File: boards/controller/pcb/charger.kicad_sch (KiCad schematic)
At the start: 44 parts, among them J4001 Battery, Q4001 BSS138, U4001 3.6, U4002 BQ25792RQMR

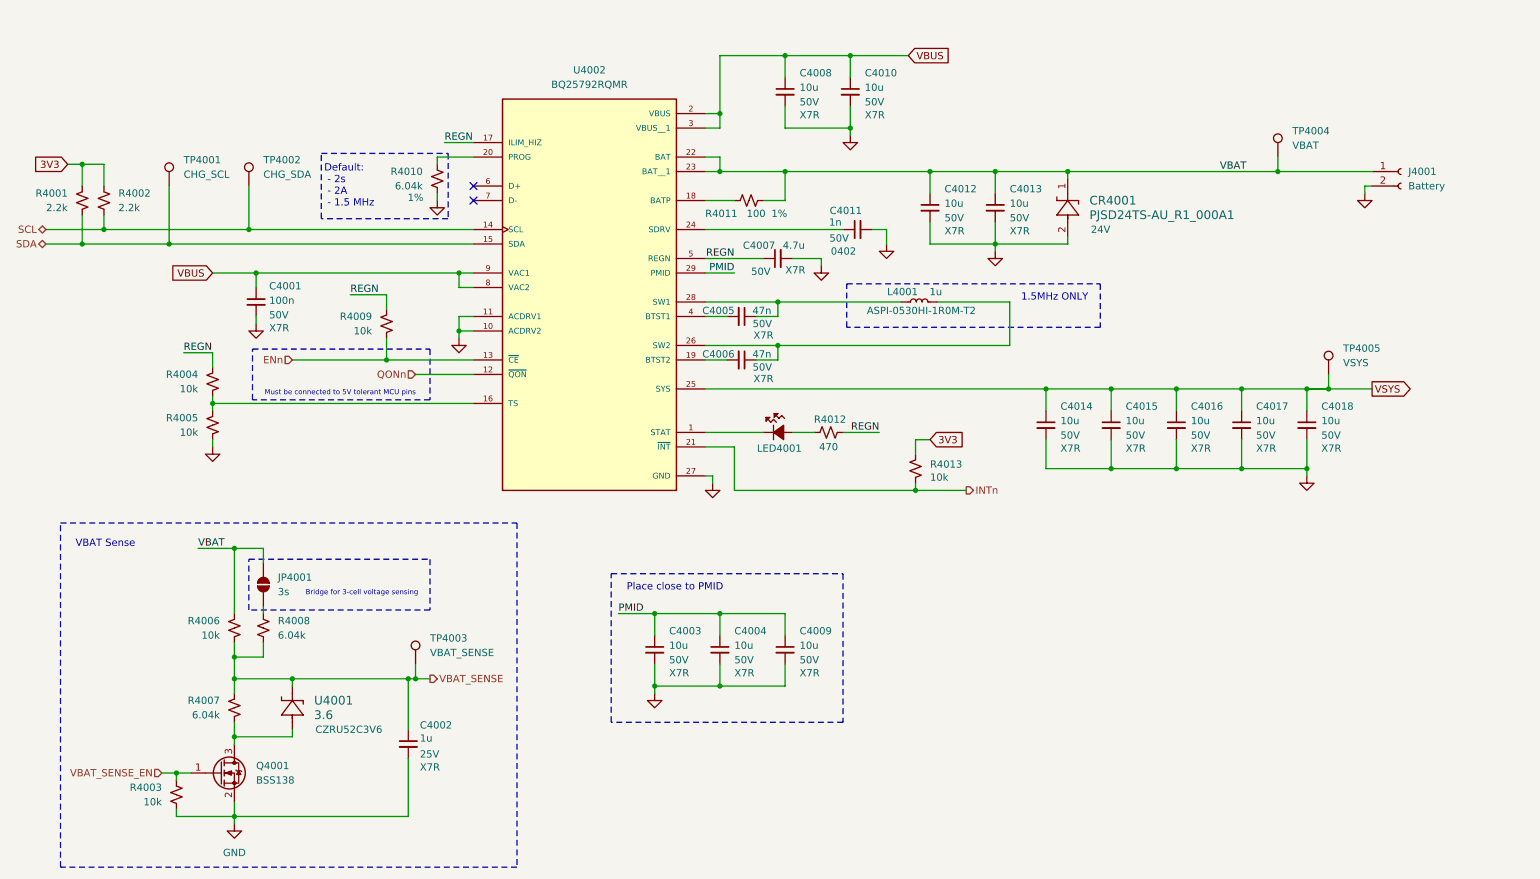
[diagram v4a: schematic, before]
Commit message: controller: Update BOM
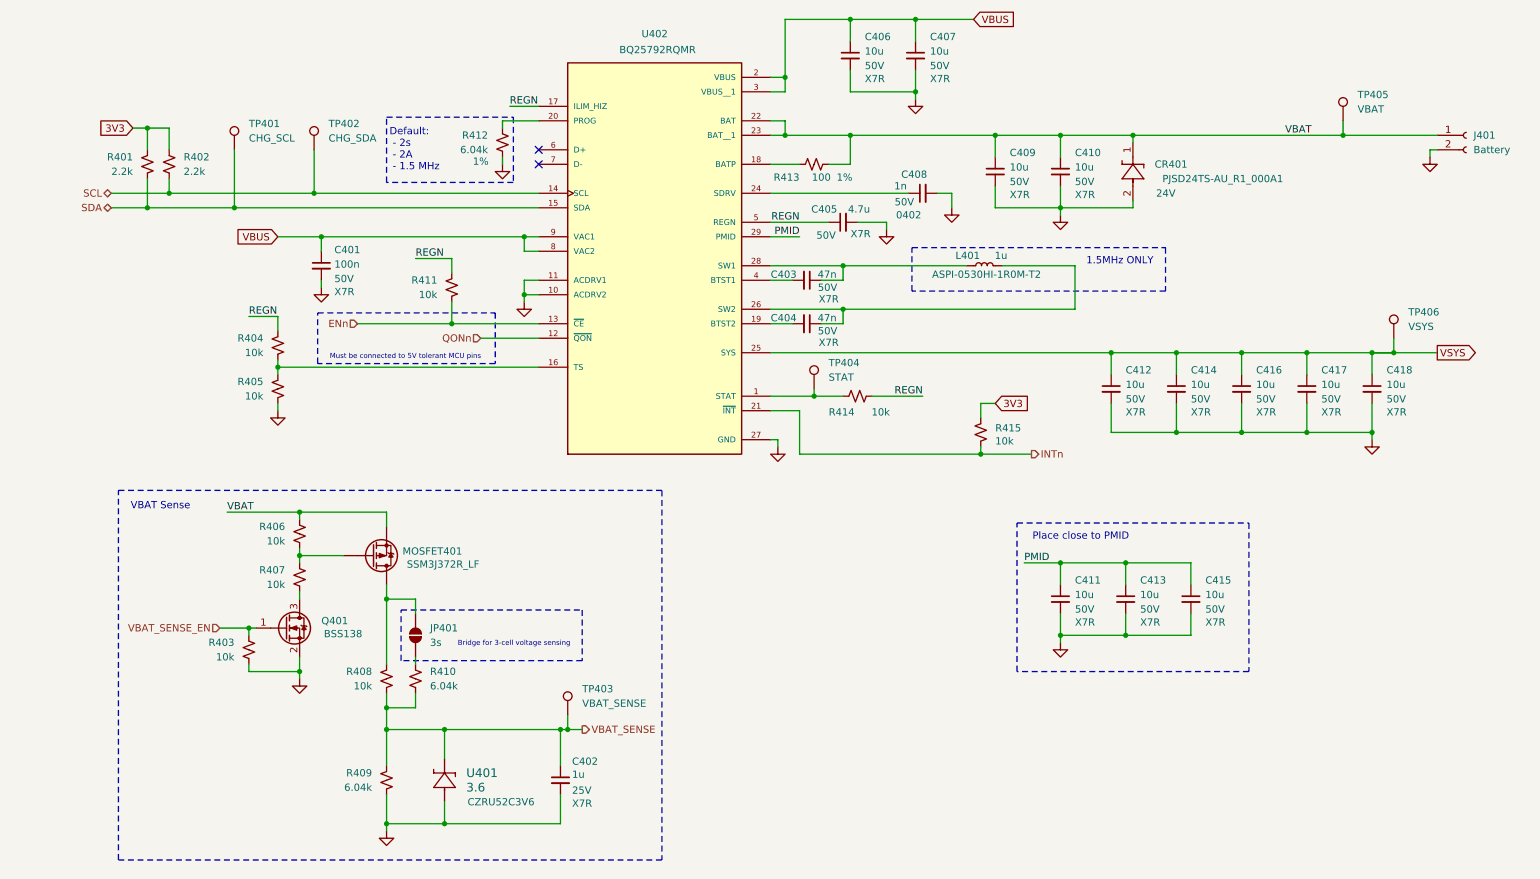
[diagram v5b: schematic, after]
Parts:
- removed LED4001: B1911PG--20D000514U1930, B1911PG--20D000514U1930:B1911PG--20D000514U1930, symbol B1911PG--20D000514U1930:B1911PG--20D000514U1930
- removed Q4001: BSS138, Package_TO_SOT_SMD:SOT-23, symbol Transistor_FET:BSS138
- removed R4012: 470, Resistor_SMD:R_0603_1608Metric, symbol Device:R_Small_US
- added MOSFET401: SSM3J372R_LF, SSM3J372R_LF:SSM3J372R_LF, symbol SSM3J372R_LF:SSM3J372R_LF
- added Q401: BSS138, Package_TO_SOT_SMD:SOT-23, symbol Transistor_FET:BSS138
- added R403, R407, R414: 10k, Resistor_SMD:R_0402_1005Metric, symbol Device:R_Small_US
- added TP404: STAT, TestPoint:TestPoint_Pad_D1.0mm, symbol Connector:TestPoint
- CR401: renamed from CR4001; MPN (none) -> PJSD24TS-AU_R1_000A1
- R401: renamed from R4001; footprint Resistor_SMD:R_0603_1608Metric -> Resistor_SMD:R_0402_1005Metric
- R402: renamed from R4002; footprint Resistor_SMD:R_0603_1608Metric -> Resistor_SMD:R_0402_1005Metric
- U402: renamed from U4002; MPN (none) -> BQ25792RQMR
- renumbered C4001 to C401, C4002 to C402, C4005 to C403, C4006 to C404, C4007 to C405, C4008 to C406, C4010 to C407, C4011 to C408, C4012 to C409, C4013 to C410, C4003 to C411, C4014 to C412, C4004 to C413, C4015 to C414, C4009 to C415, C4016 to C416, C4017 to C417, C4018 to C418, J4001 to J401, JP4001 to JP401, L4001 to L401, R4004 to R404, R4005 to R405, R4003 to R406, R4006 to R408, R4007 to R409, R4008 to R410, R4009 to R411, R4010 to R412, R4011 to R413, R4013 to R415, TP4001 to TP401, TP4002 to TP402, TP4003 to TP403, TP4004 to TP405, TP4005 to TP406, U4001 to U401
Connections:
- net GND: now also R409.2, U401.2, Q401.2 (S), R403.2; no longer R406.2
- net REGN: now also R414.2
- net VBAT: now also R406.1, MOSFET401.2 (S); no longer JP401.2 (B), R408.1
- net VBAT_SENSE_EN: now also Q401.1 (G), R403.1; no longer R406.1
- net at U402.1 (STAT): now also R414.1, TP404.1
- new net: JP401.2 (B), MOSFET401.3 (D), R408.1
- new net: MOSFET401.1 (G), R406.2, R407.1
- new net: Q401.3 (D), R407.2
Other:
- moved on the sheet: C401, C402, C403, C404, C405, C406, C407, C408, C409, C410, C411, C412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
